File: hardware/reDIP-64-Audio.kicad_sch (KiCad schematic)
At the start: 9 parts, among them U9 SGTL5000XNLA3

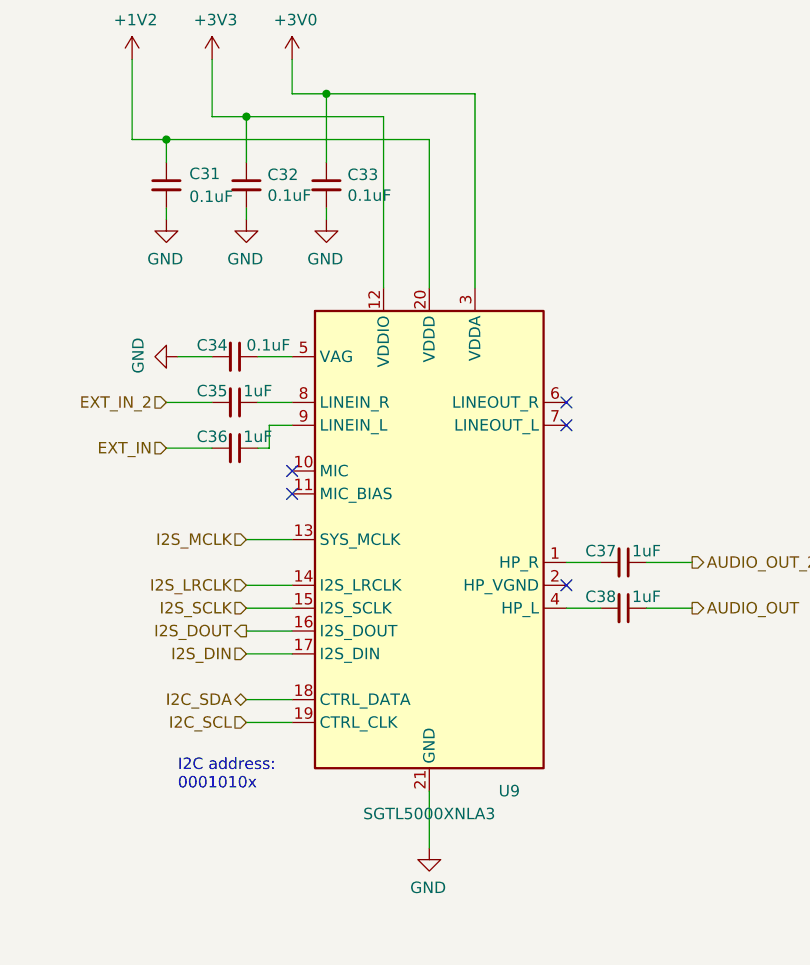
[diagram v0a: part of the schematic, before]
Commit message: Various improvements
* Removed slash from sheet names
* Reannotated schematics
* Example derivation of clocks in schematics
* Identical capacitors for DisplayPort main lanes and AUX
* Replaced switch FSA2259UMX with FSUSB42UMX
* Modified PCB physical stackup to (hopefully) be manufacturable
* Only one microvia size (0.1mm)
* Changed track width for differential pairs
* Routing cleanups and improvements
* Added files for manufacture
* Updated README

Many thanks for advice and help go to @azonenberg, @DX-MON, @gatecat,
@smunaut, and @zyp.
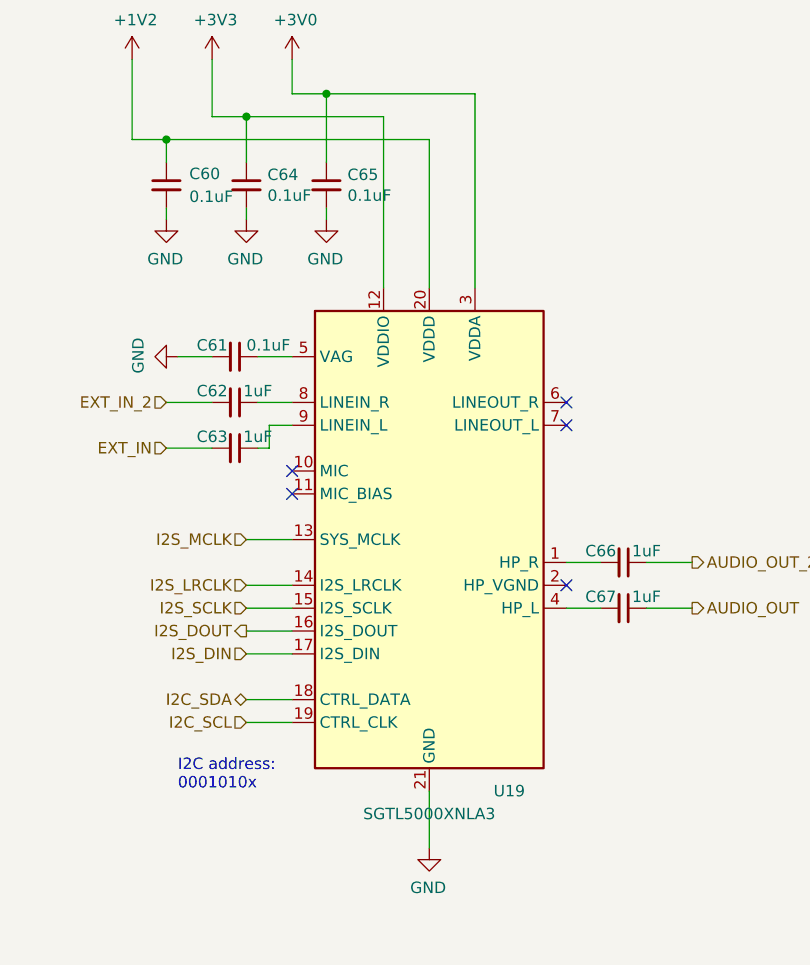
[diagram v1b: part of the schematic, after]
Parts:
- renumbered C31 to C60, C34 to C61, C35 to C62, C36 to C63, C32 to C64, C33 to C65, C37 to C66, C38 to C67, U9 to U19
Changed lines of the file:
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@@
   (title_block
     (title "reDIP 64")
-    (date "2021-05-09")
-    (rev "0.1")
+    (date "2021-06-12")
+    (rev "0.2")
     (company "Nimrod")
     (comment 1 "© 2021 Dag Lem")
@@
   (symbol (lib_id "power:+1V2") (at 121.92 52.07 0) (unit 1)
     (in_bom yes) (on_board yes)
-    (property "Reference" "#PWR051" (id 0) (at 121.92 55.88 0)
+    (property "Reference" "#PWR0129" (id 0) (at 121.92 55.88 0)
       (effects (font (size 1.27 1.27)) hide)
     )
@@
   (symbol (lib_id "power:+3V3") (at 130.81 52.07 0) (unit 1)
     (in_bom yes) (on_board yes)
-    (property "Reference" "#PWR052" (id 0) (at 130.81 55.88 0)
+    (property "Reference" "#PWR0132" (id 0) (at 130.81 55.88 0)
       (effects (font (size 1.27 1.27)) hide)
     )
@@
   (symbol (lib_id "power:+3V0") (at 139.7 52.07 0) (unit 1)
     (in_bom yes) (on_board yes)
-    (property "Reference" "#PWR053" (id 0) (at 139.7 55.88 0)
+    (property "Reference" "#PWR0134" (id 0) (at 139.7 55.88 0)
       (effects (font (size 1.27 1.27)) hide)
     )
@@
   (symbol (lib_id "power:GND") (at 125.73 69.85 0) (mirror y) (unit 1)
     (in_bom yes) (on_board yes)
-    (property "Reference" "#PWR054" (id 0) (at 125.73 76.2 0)
+    (property "Reference" "#PWR0130" (id 0) (at 125.73 76.2 0)
       (effects (font (size 1.27 1.27)) hide)
     )
@@
   (symbol (lib_id "power:GND") (at 127 85.09 270) (mirror x) (unit 1)
     (in_bom yes) (on_board yes)
-    (property "Reference" "#PWR057" (id 0) (at 120.65 85.09 0)
+    (property "Reference" "#PWR0131" (id 0) (at 120.65 85.09 0)
       (effects (font (size 1.27 1.27)) hide)
     )
@@
   (symbol (lib_id "power:GND") (at 134.62 69.85 0) (mirror y) (unit 1)
     (in_bom yes) (on_board yes)
-    (property "Reference" "#PWR055" (id 0) (at 134.62 76.2 0)
+    (property "Reference" "#PWR0133" (id 0) (at 134.62 76.2 0)
       (effects (font (size 1.27 1.27)) hide)
     )
@@
   (symbol (lib_id "power:GND") (at 143.51 69.85 0) (mirror y) (unit 1)
     (in_bom yes) (on_board yes)
-    (property "Reference" "#PWR056" (id 0) (at 143.51 76.2 0)
+    (property "Reference" "#PWR0135" (id 0) (at 143.51 76.2 0)
       (effects (font (size 1.27 1.27)) hide)
     )
@@
   (symbol (lib_id "power:GND") (at 154.94 139.7 0) (mirror y) (unit 1)
     (in_bom yes) (on_board yes)
-    (property "Reference" "#PWR058" (id 0) (at 154.94 146.05 0)
+    (property "Reference" "#PWR0136" (id 0) (at 154.94 146.05 0)
       (effects (font (size 1.27 1.27)) hide)
     )
@@
   (symbol (lib_id "Device:C_Small") (at 125.73 66.04 0) (unit 1)
     (in_bom yes) (on_board yes)
-    (property "Reference" "C31" (id 0) (at 128.27 64.77 0)
+    (property "Reference" "C60" (id 0) (at 128.27 64.77 0)
       (effects (font (size 1.27 1.27)) (justify left))
     )
@@
   (symbol (lib_id "Device:C_Small") (at 133.35 85.09 270) (unit 1)
     (in_bom yes) (on_board yes)
-    (property "Reference" "C34" (id 0) (at 130.81 83.82 90))
+    (property "Reference" "C61" (id 0) (at 130.81 83.82 90))
     (property "Value" "0.1uF" (id 1) (at 134.62 83.82 90)
       (effects (font (size 1.27 1.27)) (justify left))
@@
   (symbol (lib_id "Device:C_Small") (at 133.35 90.17 270) (unit 1)
     (in_bom yes) (on_board yes)
-    (property "Reference" "C35" (id 0) (at 130.81 88.9 90))
+    (property "Reference" "C62" (id 0) (at 130.81 88.9 90))
     (property "Value" "1uF" (id 1) (at 135.89 88.9 90))
     (property "Footprint" "Capacitor_SMD:C_0201_0603Metric" (id 2) (at 133.35 90.17 0)
@@
   (symbol (lib_id "Device:C_Small") (at 133.35 95.25 270) (unit 1)
     (in_bom yes) (on_board yes)
-    (property "Reference" "C36" (id 0) (at 130.81 93.98 90))
+    (property "Reference" "C63" (id 0) (at 130.81 93.98 90))
     (property "Value" "1uF" (id 1) (at 135.89 93.98 90))
     (property "Footprint" "Capacitor_SMD:C_0201_0603Metric" (id 2) (at 133.35 95.25 0)
@@
   (symbol (lib_id "Device:C_Small") (at 134.62 66.04 0) (unit 1)
     (in_bom yes) (on_board yes)
-    (property "Reference" "C32" (id 0) (at 136.9568 64.8716 0)
+    (property "Reference" "C64" (id 0) (at 136.9568 64.8716 0)
       (effects (font (size 1.27 1.27)) (justify left))
     )
@@
   (symbol (lib_id "Device:C_Small") (at 143.51 66.04 0) (unit 1)
     (in_bom yes) (on_board yes)
-    (property "Reference" "C33" (id 0) (at 145.8468 64.8716 0)
+    (property "Reference" "C65" (id 0) (at 145.8468 64.8716 0)
       (effects (font (size 1.27 1.27)) (justify left))
     )
@@
   (symbol (lib_id "Device:C_Small") (at 176.53 107.95 270) (unit 1)
     (in_bom yes) (on_board yes)
-    (property "Reference" "C37" (id 0) (at 173.99 106.68 90))
+    (property "Reference" "C66" (id 0) (at 173.99 106.68 90))
     (property "Value" "1uF" (id 1) (at 179.07 106.68 90))
     (property "Footprint" "Capacitor_SMD:C_0201_0603Metric" (id 2) (at 176.53 107.95 0)
@@
   (symbol (lib_id "Device:C_Small") (at 176.53 113.03 270) (unit 1)
     (in_bom yes) (on_board yes)
-    (property "Reference" "C38" (id 0) (at 173.99 111.76 90))
+    (property "Reference" "C67" (id 0) (at 173.99 111.76 90))
     (property "Value" "1uF" (id 1) (at 179.07 111.76 90))
     (property "Footprint" "Capacitor_SMD:C_0201_0603Metric" (id 2) (at 176.53 113.03 0)
@@
   (symbol (lib_id "reDIP:Nimrod-Logo-N") (at 276.86 177.8 0) (unit 1)
     (in_bom yes) (on_board yes)
-    (property "Reference" "#LOGO3" (id 0) (at 276.86 170.815 0)
+    (property "Reference" "#LOGO6" (id 0) (at 276.86 170.815 0)
       (effects (font (size 1.27 1.27)) hide)
     )
@@
   (symbol (lib_id "Audio:SGTL5000XNLA3") (at 154.94 105.41 0) (unit 1)
     (in_bom yes) (on_board yes)
-    (property "Reference" "U9" (id 0) (at 163.83 133.35 0))
+    (property "Reference" "U19" (id 0) (at 163.83 133.35 0))
     (property "Value" "SGTL5000XNLA3" (id 1) (at 154.94 135.89 0))
     (property "Footprint" "Package_DFN_QFN:QFN-20-1EP_3x3mm_P0.4mm_EP1.65x1.65mm" (id 2) (at 154.94 105.41 0)

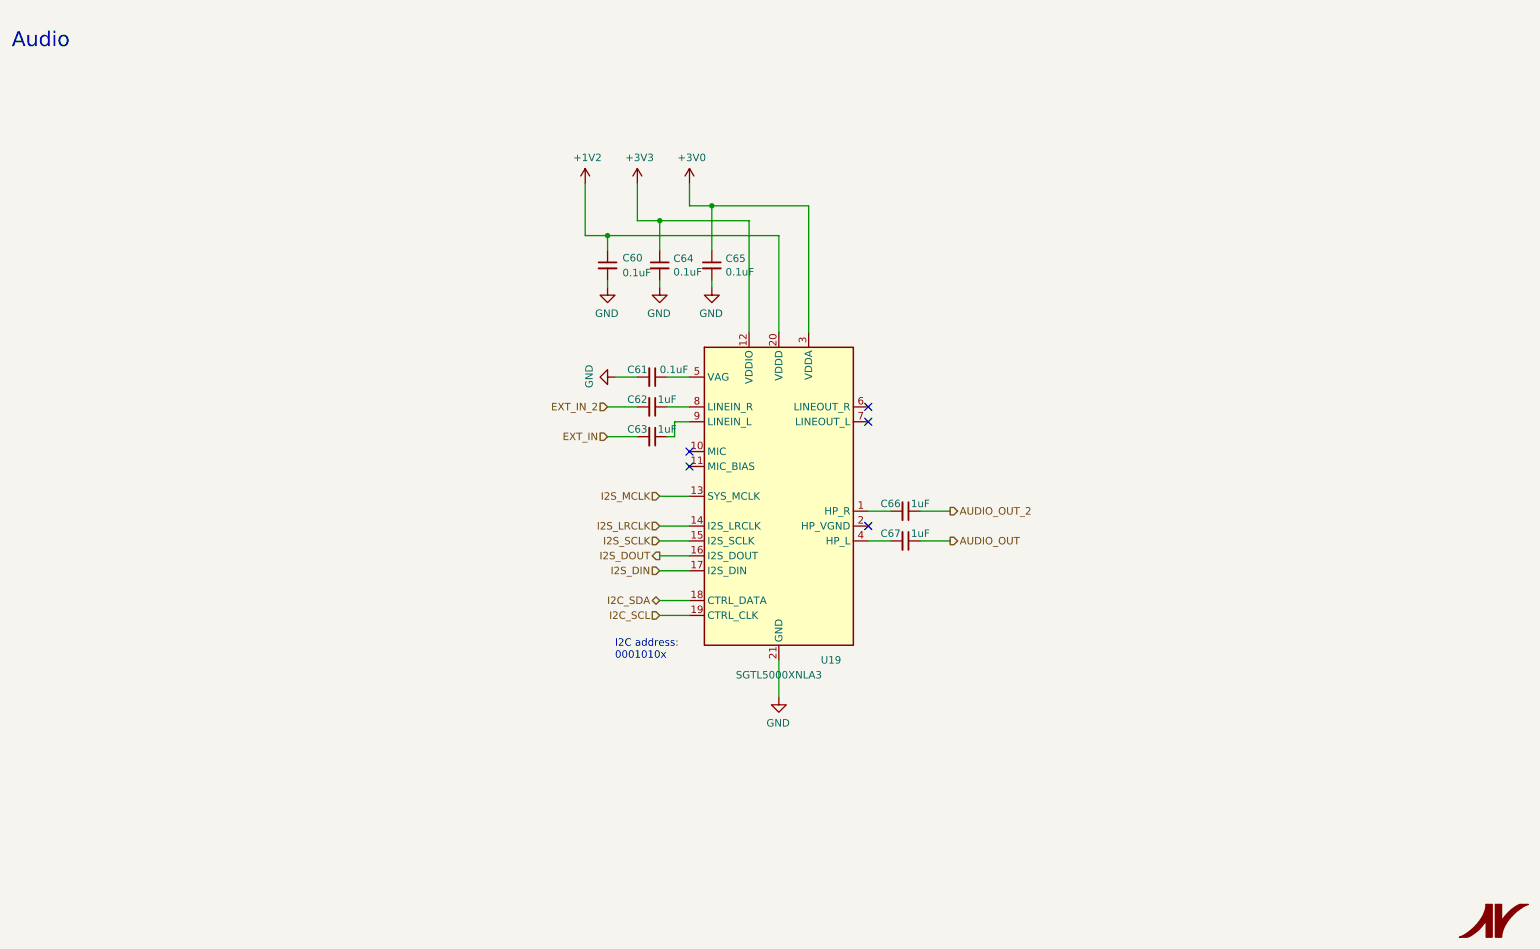
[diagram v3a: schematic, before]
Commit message: Revision 1.0
* USB receptacle replaced with GCT USB4080-03-A / HRO TYPE-C-31-M-05
* USB PD TCPC changed to PTN5110NHQ (FPF2286 has 15ms VBUS debounce time)
* Complete rework of power section
  - Over-voltage protection on VBUS (FPF2286 / FPF2495C)
  - Bidirectional VCC (2 x TPS22916)
  - Replaced EOLed buck converters with FAN53610 / FAN53611
  - Replaced EOLed LDO for ECP5 VCCAUX with NCP115AMX250TCG
  - Replaced LDO for SGTL5000 VDDA with 3.3V version
  - Added separate LDO for SGTL5000 VDDD, avoiding overvoltage on ECP5 VCC
* Bus switch changed to SN74CBT16211A, biased for level shifting
* Registered I/O for FLASH / HyperRAM clock
* Pin header changes:
  - Machined (round) pins for MOS6510 socket
  - Top only headers for additional I/O
  - Reworked pinout for VIC-II and SID
  - Removed 5V output (now available on bidirectional VCC)
  - Added GND for audio / 3.3V
  - Changed JTAG pinout to match Tag-Connect TC-LATTICE / TC-XILINX6
* Removed EXT_IN capacitors
* Button force changed from 240gf to 100gf
* Space for UL and date codes
* Black solder mask
* Silk screen updates
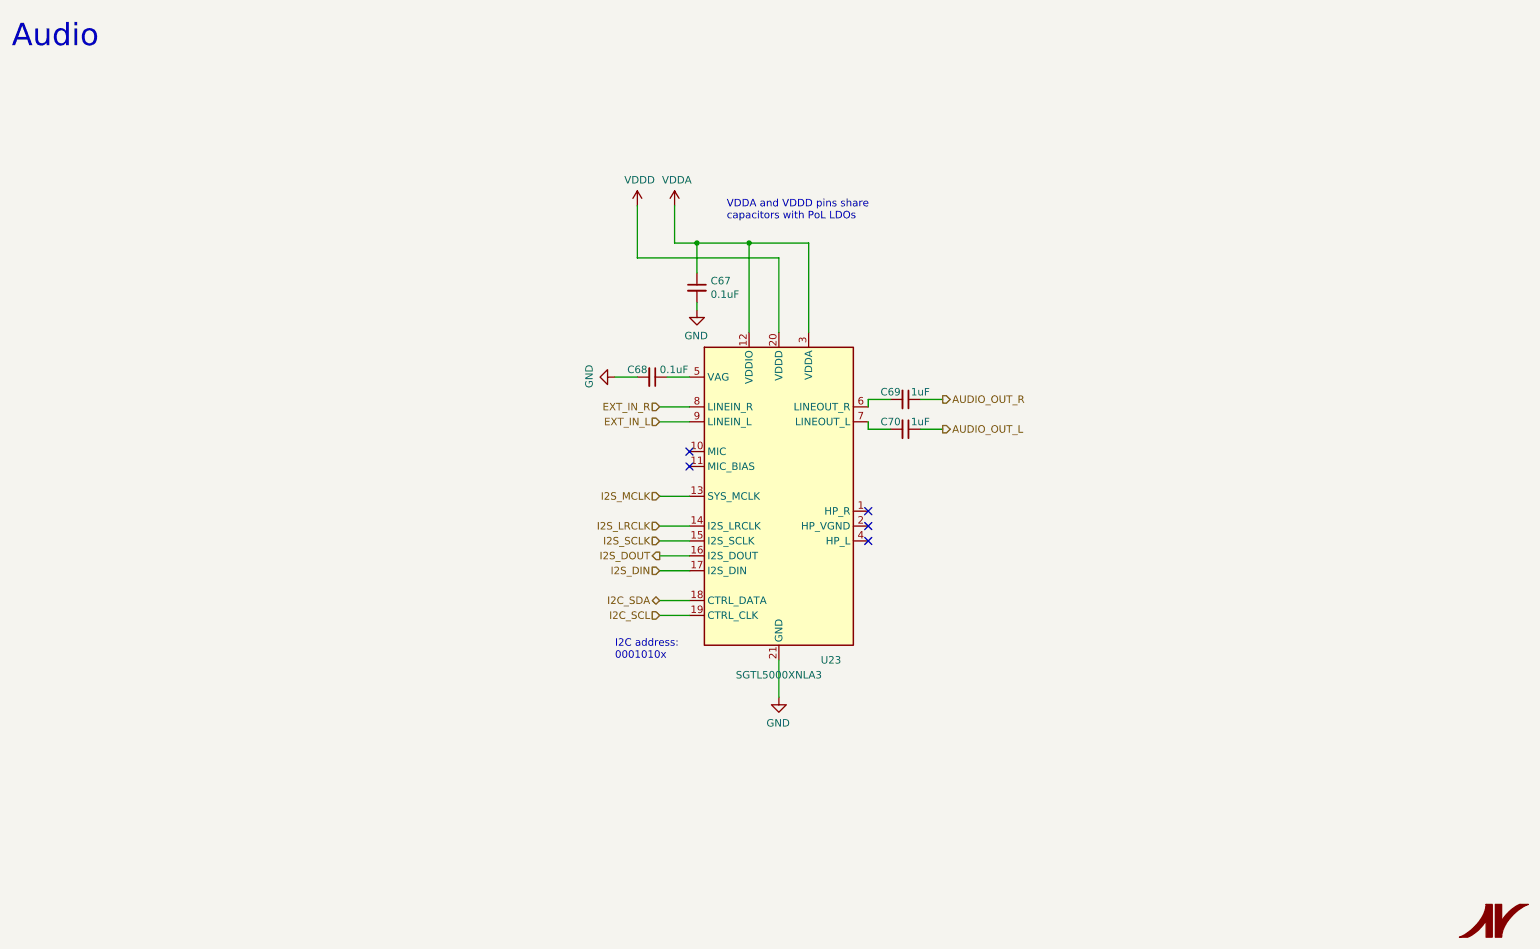
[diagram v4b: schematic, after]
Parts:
- removed C60, C65: 0.1uF, Capacitor_SMD:C_0201_0603Metric, symbol Device:C_Small
- removed C62, C63: 1uF, Capacitor_SMD:C_0201_0603Metric, symbol Device:C_Small
- U23: renamed from U19; Notes (none) -> ALTERNATIVE PART #: SGTL5000XNLA3R2; PN SGTL5000XNLA3R2 -> SGTL5000XNLA3
- renumbered C64 to C67, C61 to C68, C66 to C69, C67 to C70
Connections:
- net +3V3 is gone; now on net VDDA: C67.1, U23.12 (VDDIO)
- net at U23.1 (HP_R): no longer C69.2
- net at U23.4 (HP_L): no longer C70.2
- net at U23.6 (LINEOUT_R): now also C69.2
- net at U23.7 (LINEOUT_L): now also C70.2
- net EXT_IN_R: now reaches U23.8 (LINEIN_R)
- net EXT_IN_L: now reaches U23.9 (LINEIN_L)
- net +1V2 renamed VDDD
- net +3V0 renamed VDDA
- net AUDIO_OUT renamed AUDIO_OUT_L
- net AUDIO_OUT_2 renamed AUDIO_OUT_R
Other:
- note added: "VDDA and VDDD pins share capacitors with PoL LDOs"
- moved on the sheet: C67, C69, C70

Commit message: A few improvements
* Changed MCLK pullup to 4.7k
* A few pin swaps for cleaner routing
* Example pin headers in BOM
* Replaced reduced lifetime "mobile only" capacitors
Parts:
- C69, C70: Notes 1.5V DC AUDIO -> 1.5V DC AUDIO DERATED TO 1.3uF; PN GRM033C80J105ME05D -> GRM033R60J225ME01D
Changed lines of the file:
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@@
   (title_block
     (title "reDIP 64")
-    (date "2022-04-10")
+    (date "2022-04-14")
     (rev "1.0")
     (company "Nimrod")
@@
       (effects (font (size 1.27 1.27)) hide)
     )
-    (property "Datasheet" "https://www.murata.com/products/productdetail.aspx?partno=GRM033C80J105ME05D" (id 3) (at 176.53 88.9 0)
+    (property "Datasheet" "https://www.murata.com/products/productdetail.aspx?partno=GRM033R60J225ME01D" (id 3) (at 176.53 88.9 0)
       (effects (font (size 1.27 1.27)) hide)
     )
@@
       (effects (font (size 1.27 1.27)) hide)
     )
-    (property "PN" "GRM033C80J105ME05D" (id 5) (at 176.53 88.9 0)
-      (effects (font (size 1.27 1.27)) hide)
-    )
-    (property "Description" "CAP CER 1uF 6.3V 20% X6S 0201" (id 6) (at 176.53 88.9 0)
-      (effects (font (size 1.27 1.27)) hide)
-    )
-    (property "Notes" "1.5V DC AUDIO" (id 7) (at 176.53 88.9 0)
+    (property "PN" "GRM033R60J225ME01D" (id 5) (at 176.53 88.9 0)
+      (effects (font (size 1.27 1.27)) hide)
+    )
+    (property "Description" "CAP CER 2.2uF 6.3V 20% X5R 0201" (id 6) (at 176.53 88.9 0)
+      (effects (font (size 1.27 1.27)) hide)
+    )
+    (property "Notes" "1.5V DC AUDIO DERATED TO 1.3uF" (id 7) (at 176.53 88.9 0)
       (effects (font (size 1.27 1.27)) hide)
     )
@@
       (effects (font (size 1.27 1.27)) hide)
     )
-    (property "Datasheet" "https://www.murata.com/products/productdetail.aspx?partno=GRM033C80J105ME05D" (id 3) (at 176.53 93.98 0)
+    (property "Datasheet" "https://www.murata.com/products/productdetail.aspx?partno=GRM033R60J225ME01D" (id 3) (at 176.53 93.98 0)
       (effects (font (size 1.27 1.27)) hide)
     )
@@
       (effects (font (size 1.27 1.27)) hide)
     )
-    (property "PN" "GRM033C80J105ME05D" (id 5) (at 176.53 93.98 0)
-      (effects (font (size 1.27 1.27)) hide)
-    )
-    (property "Description" "CAP CER 1uF 6.3V 20% X6S 0201" (id 6) (at 176.53 93.98 0)
-      (effects (font (size 1.27 1.27)) hide)
-    )
-    (property "Notes" "1.5V DC AUDIO" (id 7) (at 176.53 93.98 0)
-      (effects (font (size 1.27 1.27)) hide)
-    )
+    (property "PN" "GRM033R60J225ME01D" (id 5) (at 176.53 93.98 0)
+      (effects (font (size 1.27 1.27)) hide)
+    )
+    (property "Description" "CAP CER 2.2uF 6.3V 20% X5R 0201" (id 6) (at 176.53 93.98 0)
+      (effects (font (size 1.27 1.27)) hide)
+    )
+    (property "Notes" "1.5V DC AUDIO DERATED TO 1.3uF" (id 7) (at 176.53 93.98 0)
+      (effects (font (size 1.27 1.27)) hide)
+    )
